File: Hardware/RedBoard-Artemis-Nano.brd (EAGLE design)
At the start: 43.2 x 20.3 mm, 127 parts, among them J10 USB Female Type C Connector, J11 CORTEX_DEBUG, U1 ARTEMIS_MODULESMD, U2 MCP73831, U3 3.3V, U6 CH340E_MSOP10, Y2 32.768kHz

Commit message: Changed silk around PSWC PTH.
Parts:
- removed U$29, U$43: (no value), buzzard_labels:GND17
- U$23, U$4: device buzzard_labels (7):I#O3 -> buzzard_labels (20):PSWC4
- moved U$23 0.92 mm to (14.1, 6.99)
- moved LOGO1 0.52 mm to (14.1, 10.3), turned to 0 degrees
- moved U$4 0.40 mm to (9.53, 7.49)
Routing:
- net TXO-0: track 59.2 -> 60.0 mm
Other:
- board text added: "v10"
- board text removed: "x02"
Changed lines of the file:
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@@
 <?xml version="1.0" encoding="utf-8"?>
 <!DOCTYPE eagle SYSTEM "eagle.dtd">
-<eagle version="9.4.0">
+<eagle version="9.4.2">
 <drawing>
 <settings>
@@
 <wire x1="16.51" y1="19.05" x2="42.418" y2="19.05" width="1.27" layer="22"/>
 <wire x1="13.335" y1="19.05" x2="16.51" y2="19.05" width="1.27" layer="22"/>
-<text x="1.905" y="1.016" size="1.016" layer="16" font="vector" ratio="20" rot="MR0" align="center">x02</text>
+<text x="1.905" y="1.016" size="1.016" layer="16" font="vector" ratio="20" rot="MR0" align="center">v10</text>
 <text x="29.21" y="-21.59" size="1.778" layer="51" font="vector" ratio="20">N. Seidle</text>
 <wire x1="7.62" y1="7.3152" x2="7.62" y2="6.2992" width="0.254" layer="21"/>
@@
 <text x="62.23" y="36.83" size="1.778" layer="51" font="vector" ratio="15" align="center">0.8mm Thickness</text>
 <text x="7.874" y="9.779" size="0.762" layer="28" font="vector" ratio="15" rot="MR0">DNP</text>
+<rectangle x1="10.414" y1="7.62" x2="12.446" y2="12.7" layer="22" rot="R180"/>
+<rectangle x1="10.414" y1="7.62" x2="12.446" y2="12.7" layer="21"/>
 </plain>
 <attributes>
@@
 <element name="U$39" library="buzzard_labels" package="VIN19" value="" x="15.621" y="15.113" smashed="yes" rot="MR0"/>
 <element name="U$49" library="buzzard_labels" package="3V316" value="" x="23.368" y="15.113" smashed="yes" rot="MR0"/>
-<element name="LOGO1" library="SparkFun-Aesthetics" package="SFE_LOGO_FLAME_.1" value="SFE_LOGO_FLAME.1_INCH" x="13.589" y="10.16" smashed="yes" rot="R90"/>
+<element name="LOGO1" library="SparkFun-Aesthetics" package="SFE_LOGO_FLAME_.1" value="SFE_LOGO_FLAME.1_INCH" x="14.097" y="10.287" smashed="yes"/>
 <element name="LOGO4" library="SparkFun-Aesthetics" package="SFE_LOGO_FLAME_.1" value="SFE_LOGO_FLAME.1_INCH" x="6.35" y="5.207" smashed="yes" rot="MR0"/>
 <element name="U$13" library="buzzard_labels (11)" package="ARTEMIS6" value="" x="10.287" y="2.794" smashed="yes" rot="MR0"/>
@@
 <attribute name="VALUE" x="8.89" y="8.128" size="0.6096" layer="28" font="vector" ratio="20" rot="MR0" align="top-center"/>
 </element>
-<element name="U$4" library="buzzard_labels (7)" package="I#O3" value="" x="9.652" y="7.112" smashed="yes" rot="R90"/>
-<element name="U$43" library="buzzard_labels" package="GND17" value="" x="9.652" y="9.525" smashed="yes" rot="R90"/>
-<element name="U$23" library="buzzard_labels (7)" package="I#O3" value="" x="13.208" y="7.239" smashed="yes" rot="MR0"/>
-<element name="U$29" library="buzzard_labels" package="GND17" value="" x="13.335" y="12.954" smashed="yes" rot="MR0"/>
 <element name="TP3" library="SparkFun-Connectors" package="PAD.03X.05" value="TEST-POINT3X5" x="23.622" y="13.208" smashed="yes" rot="MR0"/>
 <element name="TP4" library="SparkFun-Connectors" package="PAD.03X.05" value="TEST-POINT3X5" x="30.099" y="12.7" smashed="yes" rot="MR0"/>
+<element name="U$4" library="buzzard_labels (20)" package="PSWC4" value="" x="9.525" y="7.493" smashed="yes" rot="R90"/>
+<element name="U$23" library="buzzard_labels (20)" package="PSWC4" value="" x="14.097" y="6.985" smashed="yes" rot="MR0"/>
 </elements>
 <signals>
@@
 <wire x1="33.57805625" y1="10.0076" x2="33.2766" y2="10.30905625" width="0.762" layer="16"/>
 <wire x1="33.57805625" y1="10.0076" x2="33.60345625" y2="10.033" width="0.762" layer="16"/>
-<via x="2.794" y="17.145" extent="1-16" drill="0.3048"/>
-<wire x1="3.302" y1="16.22" x2="3.302" y2="16.637" width="0.1524" layer="16"/>
-<wire x1="3.302" y1="16.637" x2="2.794" y2="17.145" width="0.1524" layer="16"/>
-<wire x1="2.452" y1="19.558" x2="2.452" y2="17.233" width="0.1524" layer="16"/>
-<wire x1="2.794" y1="17.145" x2="2.54" y2="17.145" width="0.1524" layer="16"/>
-<wire x1="2.54" y1="17.145" x2="2.032" y2="17.145" width="0.1524" layer="16"/>
-<wire x1="2.032" y1="17.145" x2="0.889" y2="16.002" width="0.1524" layer="16"/>
-<wire x1="0.889" y1="16.002" x2="0.889" y2="14.82" width="0.1524" layer="16"/>
-<wire x1="2.452" y1="17.233" x2="2.54" y2="17.145" width="0.1524" layer="16"/>
+<via x="2.794" y="17.399" extent="1-16" drill="0.3048"/>
+<wire x1="3.302" y1="16.22" x2="3.302" y2="16.891" width="0.1524" layer="16"/>
+<wire x1="3.302" y1="16.891" x2="2.794" y2="17.399" width="0.1524" layer="16"/>
+<wire x1="2.452" y1="19.558" x2="2.452" y2="17.399" width="0.1524" layer="16"/>
+<wire x1="2.794" y1="17.399" x2="2.452" y2="17.399" width="0.1524" layer="16"/>
+<wire x1="0.889" y1="16.129" x2="0.889" y2="14.82" width="0.1524" layer="16"/>
 <wire x1="33.60345625" y1="10.033" x2="34.163" y2="10.033" width="0.254" layer="16"/>
 <polygon width="0.1524" layer="2" isolate="0.2032">
@@
 <via x="6.985" y="9.779" extent="1-16" drill="0.3048"/>
 <via x="25.4" y="13.462" extent="1-16" drill="0.3048"/>
+<wire x1="2.794" y1="17.399" x2="2.159" y2="17.399" width="0.1524" layer="16"/>
+<wire x1="2.159" y1="17.399" x2="0.889" y2="16.129" width="0.1524" layer="16"/>
 </signal>
 <signal name="V_USB">
@@
 <wire x1="32.766" y1="8.009" x2="33.829" y2="8.009" width="0.3048" layer="16"/>
 <wire x1="33.829" y1="8.009" x2="33.948" y2="8.128" width="0.3048" layer="16"/>
-<wire x1="27.432" y1="12.7" x2="27.4176" y2="12.7" width="0.1524" layer="1"/>
 <wire x1="10.53" y1="3.84" x2="10.93" y2="4.24" width="0.1524" layer="16"/>
 <wire x1="10.93" y1="4.24" x2="10.93" y2="5.08" width="0.1524" layer="16"/>
@@
 <wire x1="2.54765625" y1="18.034" x2="3.53225625" y2="19.0186" width="0.1524" layer="1"/>
 <wire x1="2.159" y1="17.653" x2="2.54" y2="18.034" width="0.1524" layer="1"/>
-<wire x1="2.148696875" y1="10.551303125" x2="2.159" y2="10.56160625" width="0.1524" layer="1"/>
-<via x="2.148696875" y="10.551303125" extent="1-16" drill="0.3048"/>
-<wire x1="2.159" y1="10.56160625" x2="2.159" y2="17.653" width="0.1524" layer="1"/>
+<wire x1="2.402696875" y1="10.297303125" x2="2.159" y2="10.541" width="0.1524" layer="1"/>
+<via x="2.402696875" y="10.297303125" extent="1-16" drill="0.3048"/>
+<wire x1="2.159" y1="10.541" x2="2.159" y2="17.653" width="0.1524" layer="1"/>
 <wire x1="1.27" y1="11.303" x2="1.3107125" y2="11.303" width="0.1524" layer="16"/>
-<wire x1="1.3107125" y1="11.303" x2="1.4223125" y2="11.1914" width="0.1524" layer="16"/>
-<wire x1="2.6736875" y1="11.1914" x2="2.159" y2="11.1914" width="0.1524" layer="16"/>
-<wire x1="2.159" y1="11.1914" x2="1.4223125" y2="11.1914" width="0.1524" layer="16"/>
-<wire x1="2.802" y1="11.72" x2="2.802" y2="11.3197125" width="0.1524" layer="16"/>
-<wire x1="2.802" y1="11.3197125" x2="2.6736875" y2="11.1914" width="0.1524" layer="16"/>
-<wire x1="2.148696875" y1="10.551303125" x2="2.159" y2="10.56160625" width="0.1524" layer="16"/>
-<wire x1="2.159" y1="10.56160625" x2="2.159" y2="11.1914" width="0.1524" layer="16"/>
+<wire x1="1.3107125" y1="11.303" x2="1.6763125" y2="10.9374" width="0.1524" layer="16"/>
+<wire x1="2.6736875" y1="10.9374" x2="2.159" y2="10.9374" width="0.1524" layer="16"/>
+<wire x1="2.159" y1="10.9374" x2="1.6763125" y2="10.9374" width="0.1524" layer="16"/>
+<wire x1="2.802" y1="11.72" x2="2.802" y2="11.0657125" width="0.1524" layer="16"/>
+<wire x1="2.802" y1="11.0657125" x2="2.6736875" y2="10.9374" width="0.1524" layer="16"/>
+<wire x1="2.402696875" y1="10.297303125" x2="2.159" y2="10.541" width="0.1524" layer="16"/>
+<wire x1="2.159" y1="10.541" x2="2.159" y2="10.9374" width="0.1524" layer="16"/>
 <wire x1="22.9616" y1="14.47650625" x2="22.9616" y2="13.97149375" width="0.1524" layer="1"/>
 <wire x1="22.9616" y1="13.97149375" x2="22.47750625" y2="13.4874" width="0.1524" layer="1"/>
@@
 <contactref element="TP1" pad="P$1"/>
 <contactref element="J11" pad="4"/>
-<wire x1="29.9386" y1="8.2884" x2="29.972" y2="8.255" width="0.1524" layer="16"/>
 <via x="38.1" y="8.128" extent="1-16" drill="0.3048"/>
 <wire x1="38.1" y1="8.128" x2="37.846" y2="7.874" width="0.1524" layer="16"/>
@@
 <via x="5.461" y="16.256" extent="1-16" drill="0.3048"/>
 <via x="5.207" y="12.446" extent="1-16" drill="0.3048"/>
+<wire x1="5.435" y1="9.65" x2="5.435" y2="9.65" width="0" layer="19" extent="1-16"/>
+<wire x1="5.461" y1="16.256" x2="5.207" y2="12.446" width="0" layer="19" extent="1-1"/>
+<wire x1="1.255" y1="9.65" x2="5.435" y2="9.65" width="0" layer="19" extent="1-16"/>
 <wire x1="1.255" y1="9.65" x2="1.255" y2="9.65" width="0" layer="19" extent="1-16"/>
 <wire x1="1.255" y1="18.29" x2="1.255" y2="18.29" width="0" layer="19" extent="1-16"/>
-<wire x1="5.435" y1="9.65" x2="1.255" y2="9.65" width="0" layer="19" extent="1-16"/>
-<wire x1="5.435" y1="9.65" x2="5.435" y2="9.65" width="0" layer="19" extent="1-16"/>
-<wire x1="5.461" y1="16.256" x2="5.207" y2="12.446" width="0" layer="19" extent="1-1"/>
 </signal>
 <signal name="D-1">

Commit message: Adding production panels
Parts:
- U1: device Testing:ARTEMIS_FP -> SparkFun-IC-Microcontroller:ARTEMIS_FP
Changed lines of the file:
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@@
 <attribute name="VALUE" x="38.862" y="11.43" size="0.6096" layer="28" font="vector" ratio="20" rot="MR270" align="top-center"/>
 </element>
-<element name="U1" library="Testing" package="ARTEMIS_FP" value="ARTEMIS_MODULESMD" x="38.1" y="10.16" smashed="yes"/>
+<element name="U1" library="SparkFun-IC-Microcontroller" package="ARTEMIS_FP" value="ARTEMIS_MODULESMD" x="38.1" y="10.16" smashed="yes">
+<attribute name="PROD_ID" value="SUB-14415" x="38.1" y="10.16" size="1.778" layer="27" display="off"/>
+</element>
 <element name="C17" library="SparkFun-Capacitors" package="0603" value="10nF" x="0.889" y="13.97" smashed="yes" rot="MR90">
 <attribute name="NAME" x="1.651" y="13.97" size="0.6096" layer="26" font="vector" ratio="20" rot="MR90" align="bottom-center"/>

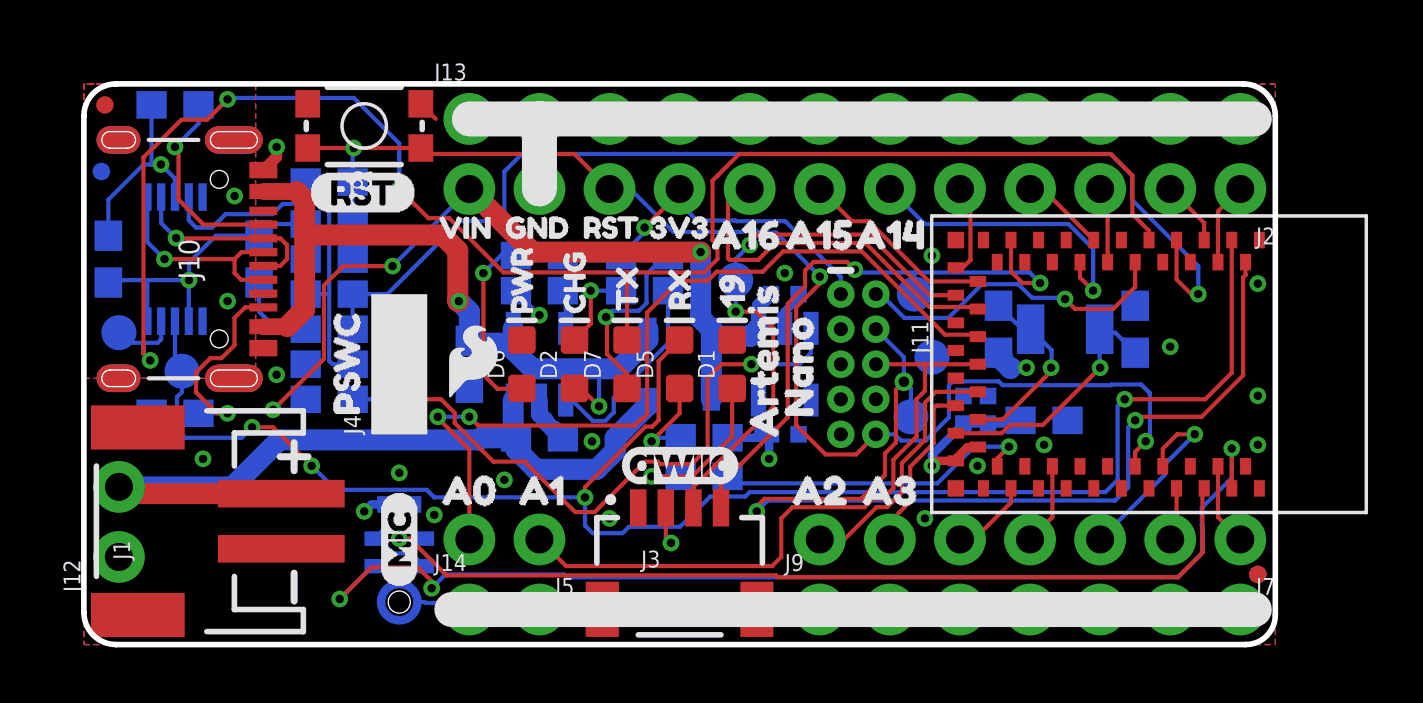
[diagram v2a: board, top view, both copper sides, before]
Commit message: Add OSHW logo
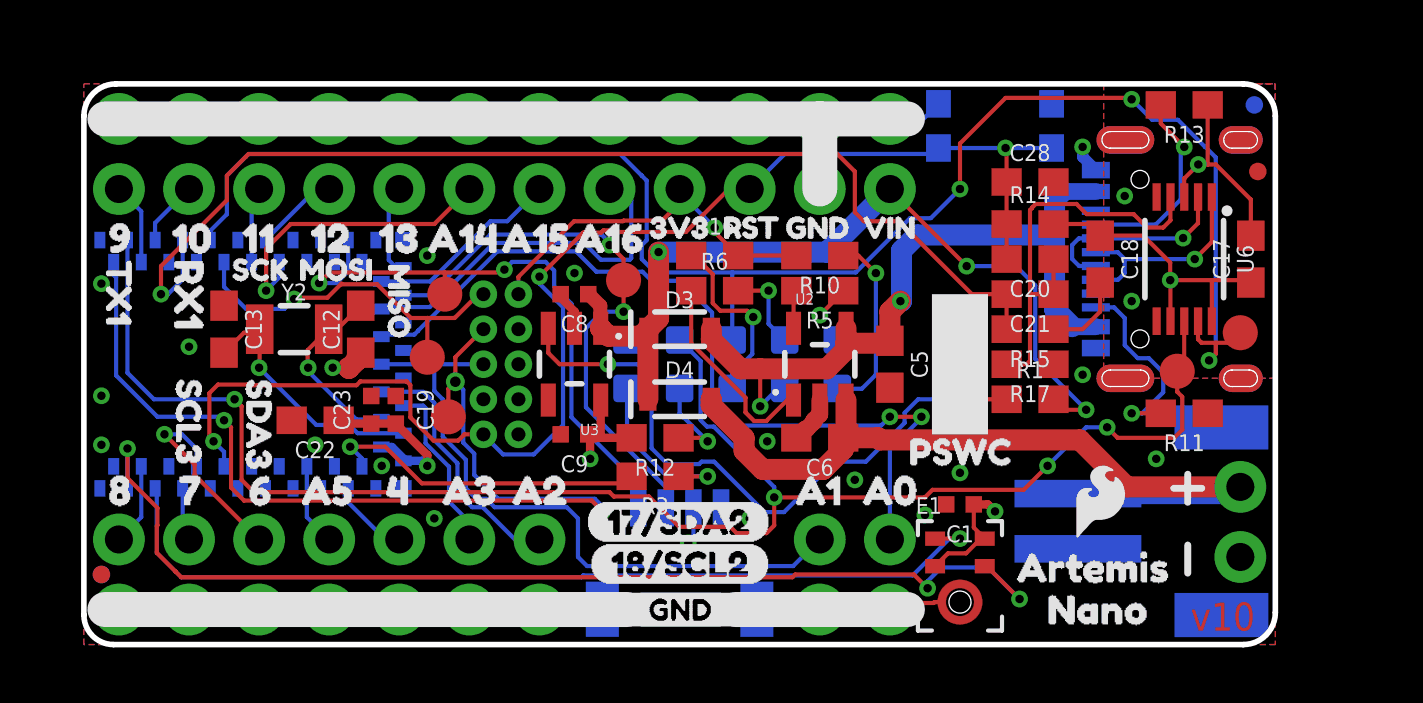
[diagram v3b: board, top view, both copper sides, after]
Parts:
- added LOGO2: OSHW-LOGONO_SILK, SparkFun-Aesthetics:DUMMY
- moved U$25 55.9 mm to (-6.35, 50.8), flipped to the bottom
- moved FRAME2 43.2 mm to (43.2, 0.00), flipped to the top
- moved U$37 43.2 mm to (0.00, 5.59), flipped to the top
- moved U$45 43.2 mm to (0.00, 14.7), flipped to the top
- moved FD1 41.9 mm to (0.64, 2.54), flipped to the bottom
- moved FD3 41.9 mm to (42.5, 17.1), flipped to the top
- moved FD4 41.9 mm to (0.64, 2.54), flipped to the top
- moved FD2 41.7 mm to (42.4, 19.6), flipped to the bottom
- moved C17 41.4 mm to (42.3, 14.0), flipped to the top
- moved J12 40.6 mm to (41.9, 3.17), flipped to the bottom
- moved J2 40.6 mm to (1.27, 16.5), flipped to the bottom
- moved J7 40.6 mm to (1.27, 3.81), flipped to the bottom
- moved TP6 40.6 mm to (41.9, 11.3), flipped to the top
- moved U$59 40.6 mm to (1.27, 14.9), flipped to the top
- moved U$46 38.6 mm to (2.29, 14.7), flipped to the top
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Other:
- outline, holes or cut-outs redrawn
